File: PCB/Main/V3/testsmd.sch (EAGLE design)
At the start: 14 parts, among them J1 FEMALE 2x3

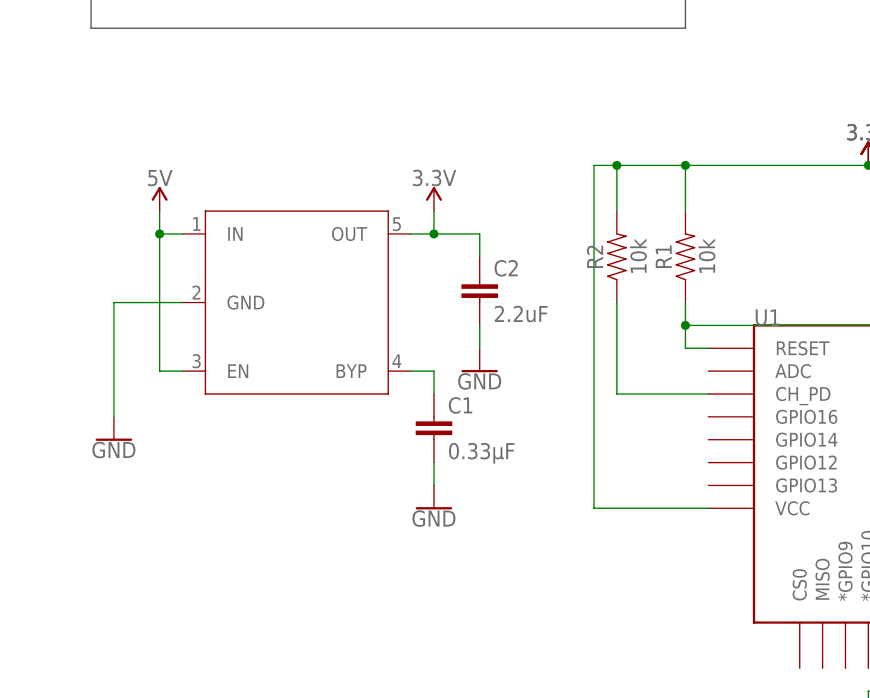
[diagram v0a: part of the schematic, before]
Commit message: Changing the board layout and adding capability to read V_BUS
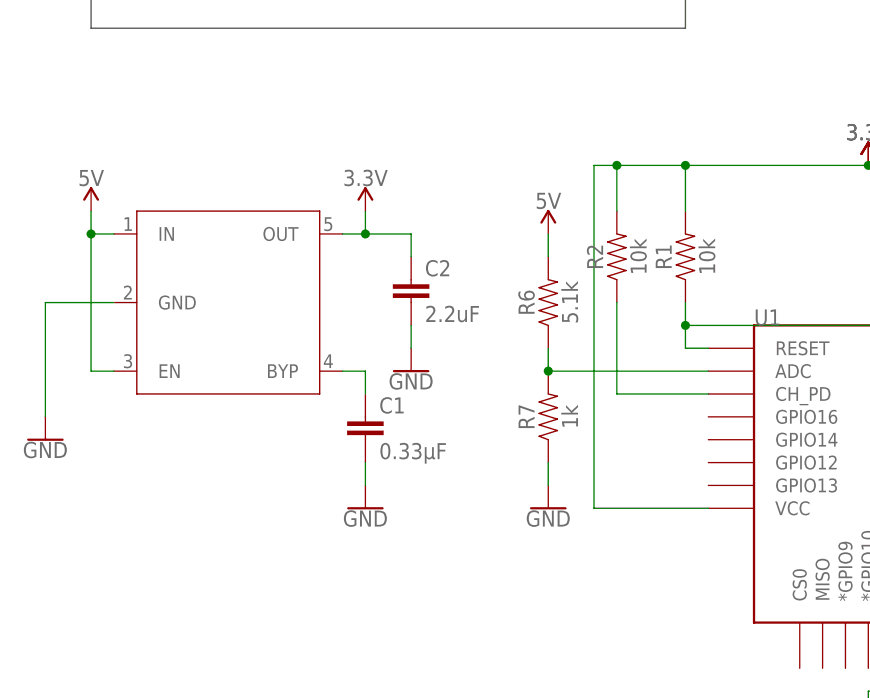
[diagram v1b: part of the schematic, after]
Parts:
- added R6: 5.1k, SparkFun-Resistors:0.75OHM-0805-1/4W-1%
- added R7: 1k, SparkFun-Resistors:0.75OHM-0805-1/4W-1%
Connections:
- new net N$9: R6.1, R7.2, U1.ADC
- net 5V: now also R6.2
- net GND: now also R7.1
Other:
- moved on the sheet: C1, C2
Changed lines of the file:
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@@
 <part name="GND12" library="SparkFun-PowerSymbols" library_urn="urn:adsk.eagle:library:530" deviceset="GND" device=""/>
 <part name="GND13" library="SparkFun-PowerSymbols" library_urn="urn:adsk.eagle:library:530" deviceset="GND" device=""/>
+<part name="SUPPLY4" library="SparkFun-PowerSymbols" library_urn="urn:adsk.eagle:library:530" deviceset="5V" device=""/>
+<part name="R6" library="SparkFun-Resistors" library_urn="urn:adsk.eagle:library:532" deviceset="0.75OHM" device="-0805-1/4W-1%" package3d_urn="urn:adsk.eagle:package:39651/1" value="5.1k"/>
+<part name="R7" library="SparkFun-Resistors" library_urn="urn:adsk.eagle:library:532" deviceset="0.75OHM" device="-0805-1/4W-1%" package3d_urn="urn:adsk.eagle:package:39651/1" value="1k"/>
+<part name="GND4" library="SparkFun-PowerSymbols" library_urn="urn:adsk.eagle:library:530" deviceset="GND" device=""/>
 </parts>
 <sheets>
@@
 <attribute name="VALUE" x="152.4" y="78.486" size="1.778" layer="96" align="top-center"/>
 </instance>
-<instance part="U$1" gate="G$1" x="0" y="83.82" smashed="yes"/>
-<instance part="SUPPLY7" gate="G$1" x="15.24" y="93.98" smashed="yes">
-<attribute name="VALUE" x="15.24" y="96.774" size="1.778" layer="96" align="bottom-center"/>
-</instance>
-<instance part="SUPPLY8" gate="G$1" x="-15.24" y="93.98" smashed="yes">
-<attribute name="VALUE" x="-15.24" y="96.774" size="1.778" layer="96" align="bottom-center"/>
-</instance>
-<instance part="GND5" gate="1" x="-20.32" y="68.58" smashed="yes">
-<attribute name="VALUE" x="-20.32" y="68.326" size="1.778" layer="96" align="top-center"/>
-</instance>
-<instance part="C1" gate="G$1" x="15.24" y="68.58" smashed="yes">
-<attribute name="NAME" x="16.764" y="71.501" size="1.778" layer="95" font="vector"/>
-<attribute name="VALUE" x="16.764" y="66.421" size="1.778" layer="96" font="vector"/>
-</instance>
-<instance part="GND3" gate="1" x="15.24" y="60.96" smashed="yes">
-<attribute name="VALUE" x="15.24" y="60.706" size="1.778" layer="96" align="top-center"/>
-</instance>
-<instance part="C2" gate="G$1" x="20.32" y="83.82" smashed="yes">
-<attribute name="NAME" x="21.844" y="86.741" size="1.778" layer="95" font="vector"/>
-<attribute name="VALUE" x="21.844" y="81.661" size="1.778" layer="96" font="vector"/>
-</instance>
-<instance part="GND6" gate="1" x="20.32" y="76.2" smashed="yes">
-<attribute name="VALUE" x="20.32" y="75.946" size="1.778" layer="96" align="top-center"/>
+<instance part="U$1" gate="G$1" x="-7.62" y="83.82" smashed="yes"/>
+<instance part="SUPPLY7" gate="G$1" x="7.62" y="93.98" smashed="yes">
+<attribute name="VALUE" x="7.62" y="96.774" size="1.778" layer="96" align="bottom-center"/>
+</instance>
+<instance part="SUPPLY8" gate="G$1" x="-22.86" y="93.98" smashed="yes">
+<attribute name="VALUE" x="-22.86" y="96.774" size="1.778" layer="96" align="bottom-center"/>
+</instance>
+<instance part="GND5" gate="1" x="-27.94" y="68.58" smashed="yes">
+<attribute name="VALUE" x="-27.94" y="68.326" size="1.778" layer="96" align="top-center"/>
+</instance>
+<instance part="C1" gate="G$1" x="7.62" y="68.58" smashed="yes">
+<attribute name="NAME" x="9.144" y="71.501" size="1.778" layer="95" font="vector"/>
+<attribute name="VALUE" x="9.144" y="66.421" size="1.778" layer="96" font="vector"/>
+</instance>
+<instance part="GND3" gate="1" x="7.62" y="60.96" smashed="yes">
+<attribute name="VALUE" x="7.62" y="60.706" size="1.778" layer="96" align="top-center"/>
+</instance>
+<instance part="C2" gate="G$1" x="12.7" y="83.82" smashed="yes">
+<attribute name="NAME" x="14.224" y="86.741" size="1.778" layer="95" font="vector"/>
+<attribute name="VALUE" x="14.224" y="81.661" size="1.778" layer="96" font="vector"/>
+</instance>
+<instance part="GND6" gate="1" x="12.7" y="76.2" smashed="yes">
+<attribute name="VALUE" x="12.7" y="75.946" size="1.778" layer="96" align="top-center"/>
 </instance>
 <instance part="U$3" gate="G$1" x="10.16" y="152.4" smashed="yes" rot="R180"/>
@@
 <instance part="GND13" gate="1" x="12.7" y="121.92" smashed="yes">
 <attribute name="VALUE" x="12.7" y="121.666" size="1.778" layer="96" align="top-center"/>
+</instance>
+<instance part="SUPPLY4" gate="G$1" x="27.94" y="91.44" smashed="yes">
+<attribute name="VALUE" x="27.94" y="94.234" size="1.778" layer="96" align="bottom-center"/>
+</instance>
+<instance part="R6" gate="G$1" x="27.94" y="83.82" smashed="yes" rot="R90">
+<attribute name="NAME" x="26.416" y="83.82" size="1.778" layer="95" font="vector" rot="R90" align="bottom-center"/>
+<attribute name="VALUE" x="29.464" y="83.82" size="1.778" layer="96" font="vector" rot="R90" align="top-center"/>
+</instance>
+<instance part="R7" gate="G$1" x="27.94" y="71.12" smashed="yes" rot="R90">
+<attribute name="NAME" x="26.416" y="71.12" size="1.778" layer="95" font="vector" rot="R90" align="bottom-center"/>
+<attribute name="VALUE" x="29.464" y="71.12" size="1.778" layer="96" font="vector" rot="R90" align="top-center"/>
+</instance>
+<instance part="GND4" gate="1" x="27.94" y="60.96" smashed="yes">
+<attribute name="VALUE" x="27.94" y="60.706" size="1.778" layer="96" align="top-center"/>
 </instance>
 </instances>
@@
 <segment>
 <pinref part="U$1" gate="G$1" pin="OUT"/>
-<wire x1="12.7" y1="91.44" x2="15.24" y2="91.44" width="0.1524" layer="91"/>
+<wire x1="5.08" y1="91.44" x2="7.62" y2="91.44" width="0.1524" layer="91"/>
 <pinref part="SUPPLY7" gate="G$1" pin="3.3V"/>
-<wire x1="15.24" y1="91.44" x2="15.24" y2="93.98" width="0.1524" layer="91"/>
+<wire x1="7.62" y1="91.44" x2="7.62" y2="93.98" width="0.1524" layer="91"/>
 <pinref part="C2" gate="G$1" pin="1"/>
-<wire x1="20.32" y1="88.9" x2="20.32" y2="91.44" width="0.1524" layer="91"/>
-<wire x1="20.32" y1="91.44" x2="15.24" y2="91.44" width="0.1524" layer="91"/>
-<junction x="15.24" y="91.44"/>
+<wire x1="12.7" y1="88.9" x2="12.7" y2="91.44" width="0.1524" layer="91"/>
+<wire x1="12.7" y1="91.44" x2="7.62" y2="91.44" width="0.1524" layer="91"/>
+<junction x="7.62" y="91.44"/>
 </segment>
 </net>
@@
 <segment>
 <pinref part="GND5" gate="1" pin="GND"/>
-<wire x1="-20.32" y1="71.12" x2="-20.32" y2="83.82" width="0.1524" layer="91"/>
+<wire x1="-27.94" y1="71.12" x2="-27.94" y2="83.82" width="0.1524" layer="91"/>
 <pinref part="U$1" gate="G$1" pin="GND"/>
-<wire x1="-20.32" y1="83.82" x2="-12.7" y2="83.82" width="0.1524" layer="91"/>
+<wire x1="-27.94" y1="83.82" x2="-20.32" y2="83.82" width="0.1524" layer="91"/>
 </segment>
 <segment>
 <pinref part="C1" gate="G$1" pin="2"/>
 <pinref part="GND3" gate="1" pin="GND"/>
-<wire x1="15.24" y1="66.04" x2="15.24" y2="63.5" width="0.1524" layer="91"/>
+<wire x1="7.62" y1="66.04" x2="7.62" y2="63.5" width="0.1524" layer="91"/>
 </segment>
 <segment>
 <pinref part="GND6" gate="1" pin="GND"/>
 <pinref part="C2" gate="G$1" pin="2"/>
-<wire x1="20.32" y1="78.74" x2="20.32" y2="81.28" width="0.1524" layer="91"/>
+<wire x1="12.7" y1="78.74" x2="12.7" y2="81.28" width="0.1524" layer="91"/>
 </segment>
 <segment>
@@
 <pinref part="R8" gate="G$1" pin="2"/>
 <wire x1="12.7" y1="124.46" x2="12.7" y2="127" width="0.1524" layer="91"/>
+</segment>
+<segment>
+<pinref part="GND4" gate="1" pin="GND"/>
+<pinref part="R7" gate="G$1" pin="1"/>
+<wire x1="27.94" y1="63.5" x2="27.94" y2="66.04" width="0.1524" layer="91"/>
 </segment>
 </net>
@@
 <segment>
 <pinref part="SUPPLY8" gate="G$1" pin="5V"/>
-<wire x1="-15.24" y1="93.98" x2="-15.24" y2="91.44" width="0.1524" layer="91"/>
+<wire x1="-22.86" y1="93.98" x2="-22.86" y2="91.44" width="0.1524" layer="91"/>
 <pinref part="U$1" gate="G$1" pin="IN"/>
-<wire x1="-15.24" y1="91.44" x2="-12.7" y2="91.44" width="0.1524" layer="91"/>
+<wire x1="-22.86" y1="91.44" x2="-20.32" y2="91.44" width="0.1524" layer="91"/>
 <pinref part="U$1" gate="G$1" pin="EN"/>
-<wire x1="-12.7" y1="76.2" x2="-15.24" y2="76.2" width="0.1524" layer="91"/>
-<wire x1="-15.24" y1="76.2" x2="-15.24" y2="91.44" width="0.1524" layer="91"/>
-<junction x="-15.24" y="91.44"/>
+<wire x1="-20.32" y1="76.2" x2="-22.86" y2="76.2" width="0.1524" layer="91"/>
+<wire x1="-22.86" y1="76.2" x2="-22.86" y2="91.44" width="0.1524" layer="91"/>
+<junction x="-22.86" y="91.44"/>
 </segment>
 <segment>
@@
 <wire x1="2.54" y1="139.7" x2="2.54" y2="165.1" width="0.1524" layer="91"/>
 </segment>
+<segment>
+<pinref part="R6" gate="G$1" pin="2"/>
+<pinref part="SUPPLY4" gate="G$1" pin="5V"/>
+<wire x1="27.94" y1="88.9" x2="27.94" y2="91.44" width="0.1524" layer="91"/>
+</segment>
 </net>
 <net name="N$8" class="0">
 <segment>
 <pinref part="U$1" gate="G$1" pin="BYP"/>
-<wire x1="12.7" y1="76.2" x2="15.24" y2="76.2" width="0.1524" layer="91"/>
+<wire x1="5.08" y1="76.2" x2="7.62" y2="76.2" width="0.1524" layer="91"/>
 <pinref part="C1" gate="G$1" pin="1"/>
-<wire x1="15.24" y1="76.2" x2="15.24" y2="73.66" width="0.1524" layer="91"/>
+<wire x1="7.62" y1="76.2" x2="7.62" y2="73.66" width="0.1524" layer="91"/>
 </segment>
 </net>
@@
 </segment>
 </net>
+<net name="N$9" class="0">
+<segment>
+<pinref part="R7" gate="G$1" pin="2"/>
+<pinref part="R6" gate="G$1" pin="1"/>
+<wire x1="27.94" y1="76.2" x2="27.94" y2="78.74" width="0.1524" layer="91"/>
+<pinref part="U1" gate="G$1" pin="ADC"/>
+<wire x1="27.94" y1="76.2" x2="45.72" y2="76.2" width="0.1524" layer="91"/>
+<junction x="27.94" y="76.2"/>
+</segment>
+</net>
